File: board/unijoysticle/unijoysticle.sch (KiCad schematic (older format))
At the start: 9 parts, among them J1 DB9_Female_MountingHoles, J2 DB9_Female_MountingHoles, J3 Barrel_Jack_MountingPin, U1 4066, U2 4066, U4 4066, U5 4066

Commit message: board: using switch for c64/amiga mouse
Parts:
- added SW1: SW_SPDT, Button_Switch_THT:SW_CuK_OS102011MA1QN1_SPDT_Angled, symbol Switch:SW_SPDT
- B1: footprint RF_Module:ESP32-WROOM-32 -> Parts:MH-ET_LIVE_MINIKIT_ESP32
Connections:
- net labels added: J1POWER, POWER_OR_GND
- net labels removed: +5V
- wire segments 42 -> 41
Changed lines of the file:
@@
 Wire Wire Line
 	1800 6900 2050 6900
-$Comp
-L power:+5V #PWR08
-U 1 1 5C693B07
-P 2350 6900
-F 0 "#PWR08" H 2350 6750 50  0001 C CNN
-F 1 "+5V" V 2365 7028 50  0000 L CNN
-F 2 "" H 2350 6900 50  0001 C CNN
-F 3 "" H 2350 6900 50  0001 C CNN
-	1    2350 6900
-	0    1    -1   0
-$EndComp
 Text GLabel 2250 1800 2    50   Input ~ 0
 GPIO_J1DOWN
@@
 Wire Wire Line
 	3650 1250 2950 1250
-$Comp
-L power:VDD #PWR0103
-U 1 1 5C6D9076
-P 2950 1250
-F 0 "#PWR0103" H 2950 1100 50  0001 C CNN
-F 1 "VDD" V 2967 1377 50  0000 L CNN
-F 2 "" H 2950 1250 50  0001 C CNN
-F 3 "" H 2950 1250 50  0001 C CNN
-	1    2950 1250
-	0    -1   1    0
-$EndComp
 Text GLabel 6800 950  2    50   Input ~ 0
 J2UP
@@
 Wire Wire Line
 	7300 1450 6800 1450
-Wire Wire Line
-	6800 1250 7300 1250
-$Comp
-L power:VDD #PWR0104
-U 1 1 5C6DCA05
-P 7300 1250
-F 0 "#PWR0104" H 7300 1100 50  0001 C CNN
-F 1 "VDD" V 7317 1378 50  0000 L CNN
-F 2 "" H 7300 1250 50  0001 C CNN
-F 3 "" H 7300 1250 50  0001 C CNN
-	1    7300 1250
-	0    1    1    0
-$EndComp
 Text GLabel 8250 950  0    50   Input ~ 0
 J2UP
@@
 	9250 4250 9450 4250
 Connection ~ 9250 4250
-$Comp
-L power:VDD #PWR0105
-U 1 1 5C6E6105
-P 9450 4250
-F 0 "#PWR0105" H 9450 4100 50  0001 C CNN
-F 1 "VDD" V 9467 4378 50  0000 L CNN
-F 2 "" H 9450 4250 50  0001 C CNN
-F 3 "" H 9450 4250 50  0001 C CNN
-	1    9450 4250
-	0    1    1    0
-$EndComp
 Text GLabel 2250 3850 2    50   Input ~ 0
 J1FIRE
@@
 Connection ~ 1250 4550
 $Comp
-L power:VDD #PWR0106
-U 1 1 5C6E8414
-P 1100 4550
-F 0 "#PWR0106" H 1100 4400 50  0001 C CNN
-F 1 "VDD" V 1118 4677 50  0000 L CNN
-F 2 "" H 1100 4550 50  0001 C CNN
-F 3 "" H 1100 4550 50  0001 C CNN
-	1    1100 4550
-	0    -1   -1   0
-$EndComp
-$Comp
 L power:GND #PWR0107
 U 1 1 5C6BCB4E
@@
 F 0 "B1" H 5250 5560 45  0000 C CNN
 F 1 "ESP32_THING_W_ANT_KEEPOUT" H 5250 5476 45  0000 C CNN
-F 2 "RF_Module:ESP32-WROOM-32" H 5250 5400 20  0001 C CNN
+F 2 "Parts:MH-ET_LIVE_MINIKIT_ESP32" H 5250 5400 20  0001 C CNN
 F 3 "" H 5250 4200 50  0001 C CNN
 F 4 "DEV-13907" H 5250 5381 60  0000 C CNN "Field4"
@@
 Wire Wire Line
 	4300 5000 4750 5000
-$Comp
-L power:+5V #PWR0108
-U 1 1 5C6C0C34
+Entry Bus Bus
+	8750 7700 8850 7800
+$Comp
+L power:VDD #PWR0103
+U 1 1 5C6BA1C1
+P 2350 6900
+F 0 "#PWR0103" H 2350 6750 50  0001 C CNN
+F 1 "VDD" V 2367 7028 50  0000 L CNN
+F 2 "" H 2350 6900 50  0001 C CNN
+F 3 "" H 2350 6900 50  0001 C CNN
+	1    2350 6900
+	0    1    1    0
+$EndComp
+$Comp
+L power:VDD #PWR0104
+U 1 1 5C6BA444
 P 4300 5000
-F 0 "#PWR0108" H 4300 4850 50  0001 C CNN
-F 1 "+5V" V 4315 5128 50  0000 L CNN
+F 0 "#PWR0104" H 4300 4850 50  0001 C CNN
+F 1 "VDD" V 4318 5127 50  0000 L CNN
 F 2 "" H 4300 5000 50  0001 C CNN
 F 3 "" H 4300 5000 50  0001 C CNN
 	1    4300 5000
-	0    -1   1    0
-$EndComp
+	0    -1   -1   0
+$EndComp
+Text GLabel 2950 1250 0    50   Input ~ 0
+J1POWER
+$Comp
+L Switch:SW_SPDT SW1
+U 1 1 5C6BA76A
+P 1650 5800
+F 0 "SW1" H 1650 6085 50  0000 C CNN
+F 1 "SW_SPDT" H 1650 5994 50  0000 C CNN
+F 2 "Button_Switch_THT:SW_CuK_OS102011MA1QN1_SPDT_Angled" H 1650 5800 50  0001 C CNN
+F 3 "" H 1650 5800 50  0001 C CNN
+	1    1650 5800
+	1    0    0    -1
+$EndComp
+Text GLabel 1850 5900 2    50   Input ~ 0
+J1POWER
+$Comp
+L power:GND #PWR0105
+U 1 1 5C6BAB57
+P 1850 5700
+F 0 "#PWR0105" H 1850 5450 50  0001 C CNN
+F 1 "GND" V 1855 5572 50  0000 R CNN
+F 2 "" H 1850 5700 50  0001 C CNN
+F 3 "" H 1850 5700 50  0001 C CNN
+	1    1850 5700
+	0    -1   -1   0
+$EndComp
+Text GLabel 1450 5800 0    50   Input ~ 0
+POWER_OR_GND
+Text GLabel 1100 4550 0    50   Input ~ 0
+POWER_OR_GND
+Text GLabel 9450 4250 2    50   Input ~ 0
+POWER_OR_GND
 $EndSCHEMATC

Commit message: board: better layout
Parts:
- J1: footprint Connector_Dsub:DSUB-9_Female_Horizontal_P2.77x2.84mm_EdgePinOffset4.94mm_Housed_MountingHolesOffset7.48mm -> Connector_Dsub:DSUB-9_Female_Horizontal_P2.77x2.84mm_EdgePinOffset9.40mm
- J2: footprint Connector_Dsub:DSUB-9_Female_Horizontal_P2.77x2.84mm_EdgePinOffset4.94mm_Housed_MountingHolesOffset7.48mm -> Connector_Dsub:DSUB-9_Female_EdgeMount_P2.77mm
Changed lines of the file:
@@
 F 0 "J1" H 4130 1353 50  0000 L CNN
 F 1 "DB9_Female_MountingHoles" H 4130 1262 50  0000 L CNN
-F 2 "Connector_Dsub:DSUB-9_Female_Horizontal_P2.77x2.84mm_EdgePinOffset4.94mm_Housed_MountingHolesOffset7.48mm" H 3950 1350 50  0001 C CNN
+F 2 "Connector_Dsub:DSUB-9_Female_Horizontal_P2.77x2.84mm_EdgePinOffset9.40mm" H 3950 1350 50  0001 C CNN
 F 3 " ~" H 3950 1350 50  0001 C CNN
 	1    3950 1350
@@
 F 0 "J2" H 6680 1353 50  0000 L CNN
 F 1 "DB9_Female_MountingHoles" H 6680 1262 50  0000 L CNN
-F 2 "Connector_Dsub:DSUB-9_Female_Horizontal_P2.77x2.84mm_EdgePinOffset4.94mm_Housed_MountingHolesOffset7.48mm" H 6500 1350 50  0001 C CNN
+F 2 "Connector_Dsub:DSUB-9_Female_EdgeMount_P2.77mm" H 6500 1350 50  0001 C CNN
 F 3 " ~" H 6500 1350 50  0001 C CNN
 	1    6500 1350

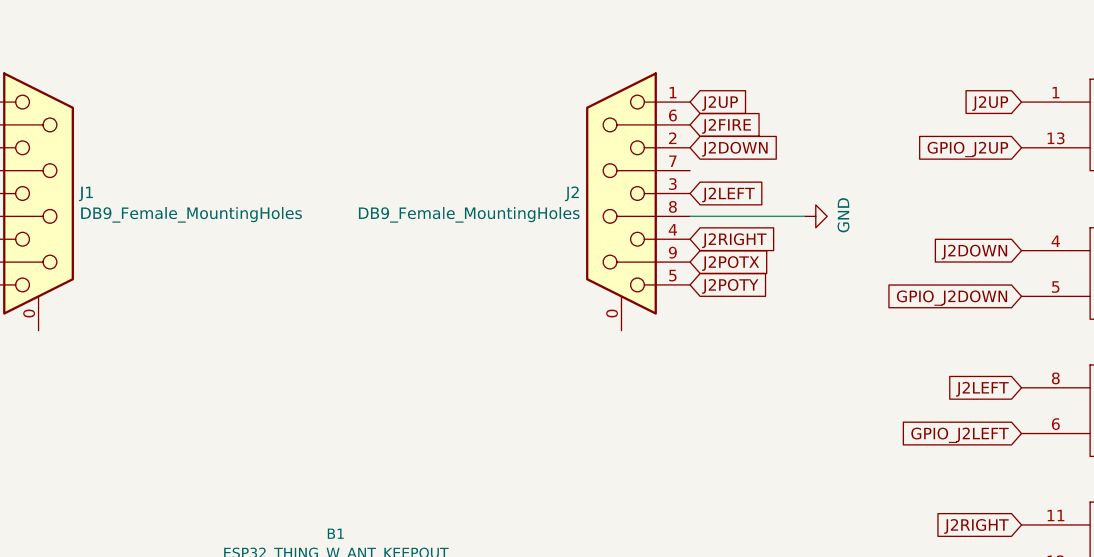
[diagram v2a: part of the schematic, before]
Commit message: board: routing added
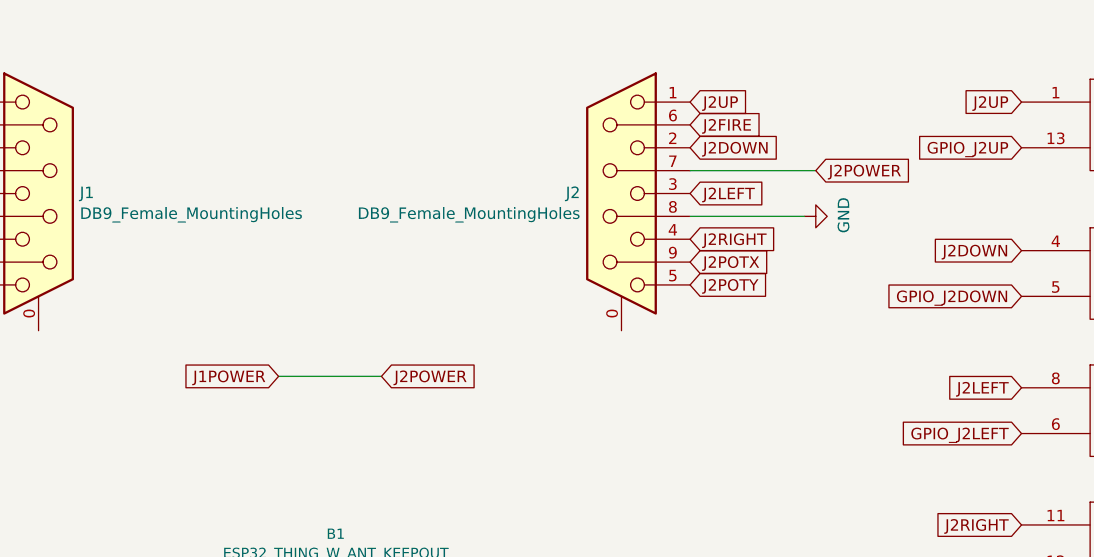
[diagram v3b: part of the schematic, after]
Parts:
- J2: footprint Connector_Dsub:DSUB-9_Female_EdgeMount_P2.77mm -> Connector_Dsub:DSUB-9_Female_Horizontal_P2.77x2.84mm_EdgePinOffset9.40mm
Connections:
- net J1POWER: now also J2.7
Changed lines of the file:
@@
 F 0 "J2" H 6680 1353 50  0000 L CNN
 F 1 "DB9_Female_MountingHoles" H 6680 1262 50  0000 L CNN
-F 2 "Connector_Dsub:DSUB-9_Female_EdgeMount_P2.77mm" H 6500 1350 50  0001 C CNN
+F 2 "Connector_Dsub:DSUB-9_Female_Horizontal_P2.77x2.84mm_EdgePinOffset9.40mm" H 6500 1350 50  0001 C CNN
 F 3 " ~" H 6500 1350 50  0001 C CNN
 	1    6500 1350
@@
 Text GLabel 9450 4250 2    50   Input ~ 0
 POWER_OR_GND
+Text GLabel 7350 1250 2    50   Input ~ 0
+J2POWER
+Wire Wire Line
+	6800 1250 7350 1250
+Text GLabel 5000 2150 0    50   Input ~ 0
+J1POWER
+Wire Wire Line
+	5000 2150 5450 2150
+Text GLabel 5450 2150 2    50   Input ~ 0
+J2POWER
 $EndSCHEMATC

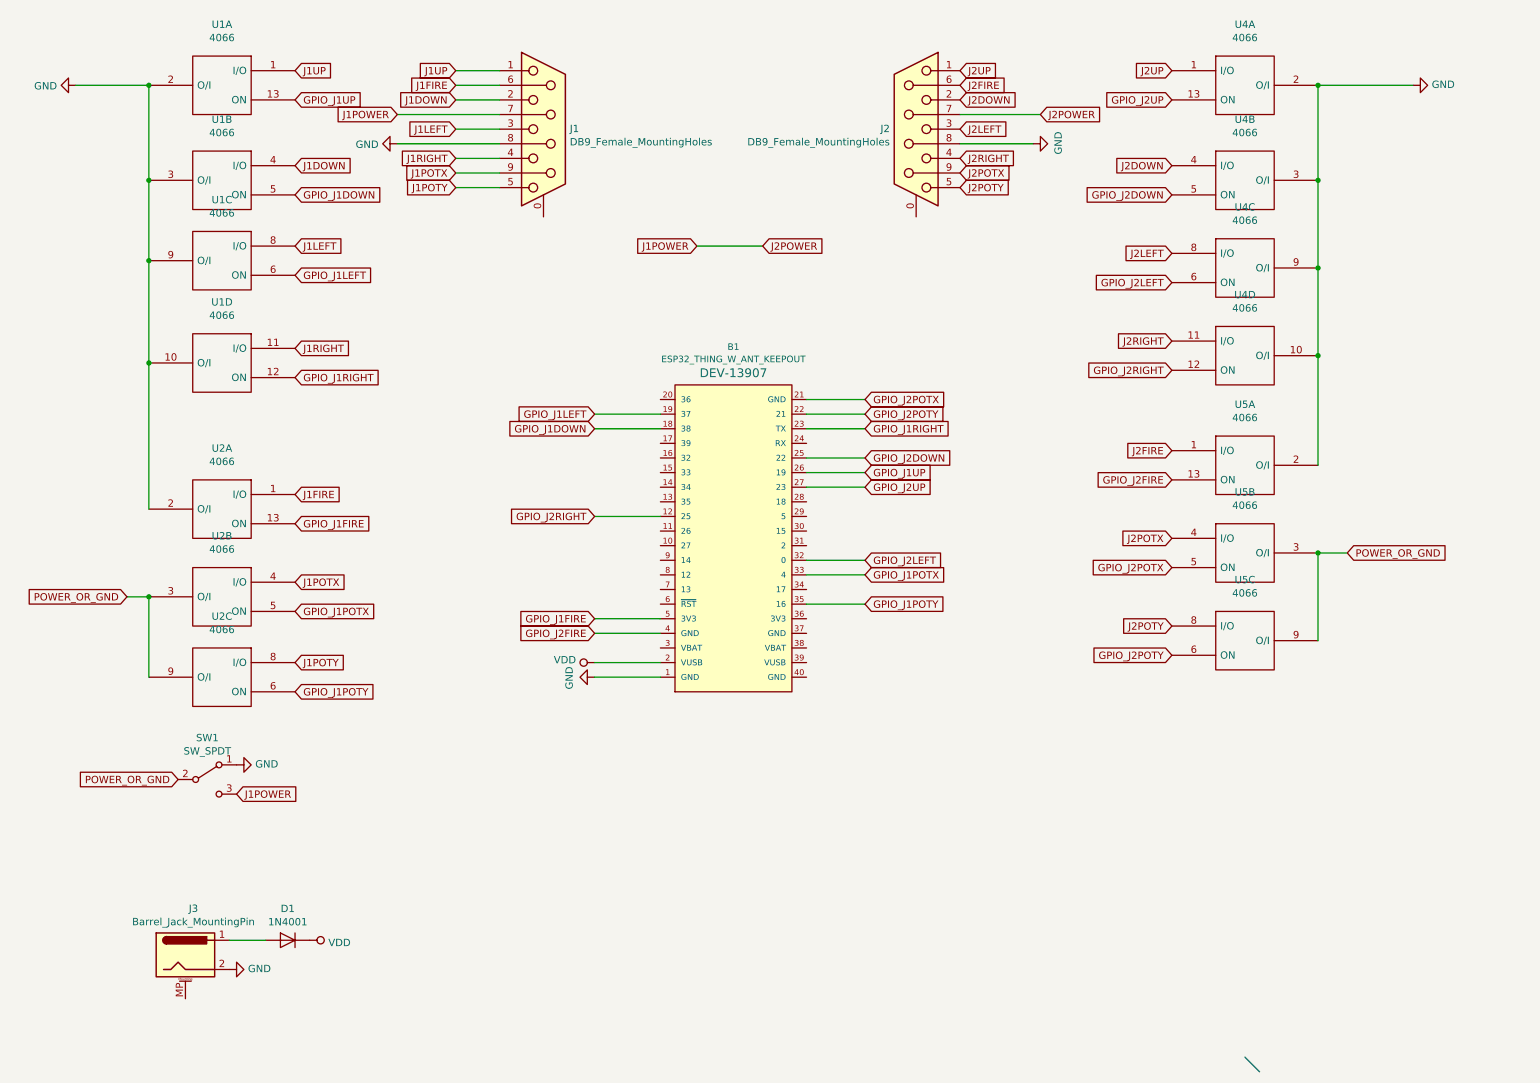
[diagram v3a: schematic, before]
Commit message: board: using new db9 female to avoid errors.
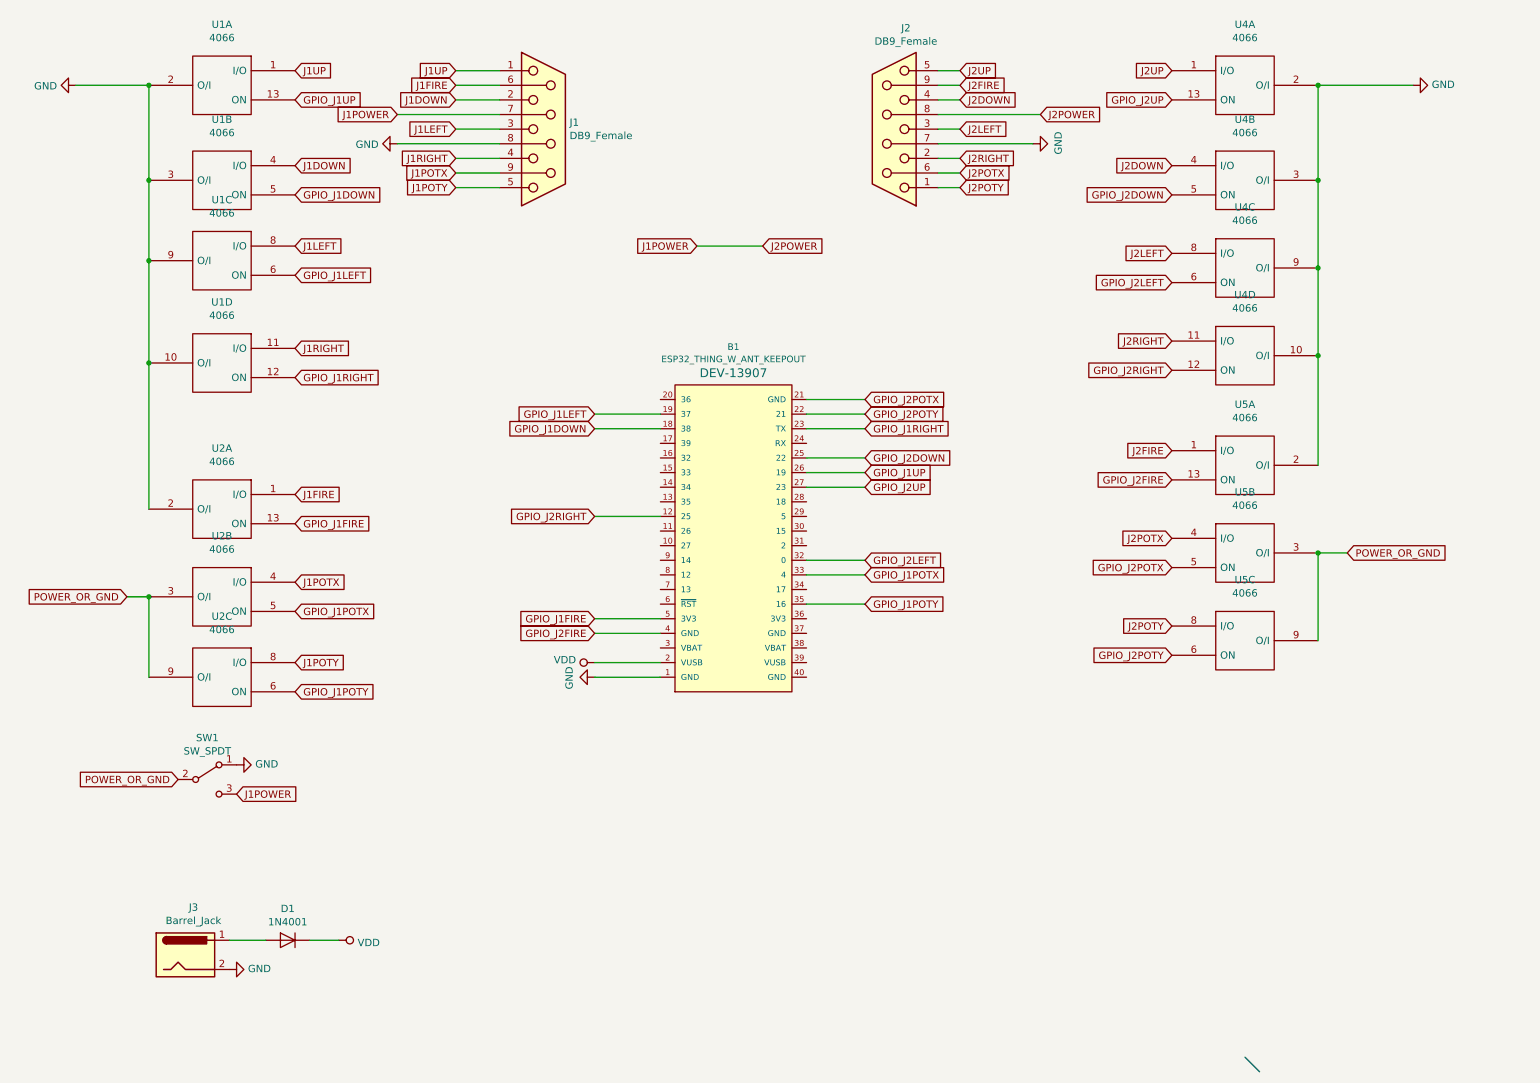
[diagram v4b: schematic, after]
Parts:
- removed J1, J2: DB9_Female_MountingHoles, Connector_Dsub:DSUB-9_Female_Horizontal_P2.77x2.84mm_EdgePinOffset9.40mm, symbol Connector:DB9_Female_MountingHoles
- removed J3: Barrel_Jack_MountingPin, Connector_BarrelJack:BarrelJack_Horizontal, symbol Connector:Barrel_Jack_MountingPin
- added J1, J2: DB9_Female, Connector_Dsub:DSUB-9_Female_Horizontal_P2.77x2.84mm_EdgePinOffset9.40mm, symbol Connector:DB9_Female
- added J3: Barrel_Jack, Connector_BarrelJack:BarrelJack_Horizontal, symbol Connector:Barrel_Jack
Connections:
- net GND: now also J1.8, J2.7, J3.2
- net J1DOWN: now also J1.2
- net J1FIRE: now also J1.6
- net J1LEFT: now also J1.3
- net J1POTX: now also J1.9
- net J1POTY: now also J1.5
- net J1POWER: now also J1.7, J2.8
- net J1RIGHT: now also J1.4
- net J1UP: now also J1.1
- net J2DOWN: now also J2.4
- net J2FIRE: now also J2.9
- net J2LEFT: now also J2.3
- net J2POTX: now also J2.6
- net J2POTY: now also J2.1
- net J2RIGHT: now also J2.2
- net J2UP: now also J2.5
- net at D1.2 (A): now also J3.1
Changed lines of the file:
@@
-$EndComp
-$Comp
-L Connector:DB9_Female_MountingHoles J1
-U 1 1 5C65A0B0
-P 3950 1350
-F 0 "J1" H 4130 1353 50  0000 L CNN
-F 1 "DB9_Female_MountingHoles" H 4130 1262 50  0000 L CNN
-F 2 "Connector_Dsub:DSUB-9_Female_Horizontal_P2.77x2.84mm_EdgePinOffset9.40mm" H 3950 1350 50  0001 C CNN
-F 3 " ~" H 3950 1350 50  0001 C CNN
-	1    3950 1350
-	1    0    0    -1
-$EndComp
-$Comp
-L Connector:DB9_Female_MountingHoles J2
-U 1 1 5C65A122
-P 6500 1350
-F 0 "J2" H 6680 1353 50  0000 L CNN
-F 1 "DB9_Female_MountingHoles" H 6680 1262 50  0000 L CNN
-F 2 "Connector_Dsub:DSUB-9_Female_Horizontal_P2.77x2.84mm_EdgePinOffset9.40mm" H 6500 1350 50  0001 C CNN
-F 3 " ~" H 6500 1350 50  0001 C CNN
-	1    6500 1350
-	-1   0    0    -1
-$EndComp
-$Comp
-L Connector:Barrel_Jack_MountingPin J3
-U 1 1 5C65A2B3
-P 1500 7000
-F 0 "J3" H 1555 7317 50  0000 C CNN
-F 1 "Barrel_Jack_MountingPin" H 1555 7226 50  0000 C CNN
-F 2 "Connector_BarrelJack:BarrelJack_Horizontal" H 1550 6960 50  0001 C CNN
-F 3 "~" H 1550 6960 50  0001 C CNN
-	1    1500 7000
-	1    0    0    -1
 $EndComp
 $Comp
@@
 Text GLabel 6800 1650 2    50   Input ~ 0
 J2POTX
-Wire Wire Line
-	7300 1450 6800 1450
 Text GLabel 8250 950  0    50   Input ~ 0
 J2UP
@@
 L power:VDD #PWR0103
 U 1 1 5C6BA1C1
-P 2350 6900
-F 0 "#PWR0103" H 2350 6750 50  0001 C CNN
-F 1 "VDD" V 2367 7028 50  0000 L CNN
-F 2 "" H 2350 6900 50  0001 C CNN
-F 3 "" H 2350 6900 50  0001 C CNN
-	1    2350 6900
+P 2550 6900
+F 0 "#PWR0103" H 2550 6750 50  0001 C CNN
+F 1 "VDD" V 2567 7028 50  0000 L CNN
+F 2 "" H 2550 6900 50  0001 C CNN
+F 3 "" H 2550 6900 50  0001 C CNN
+	1    2550 6900
 	0    1    1    0
-$EndComp
-$Comp
-L power:VDD #PWR0104
-U 1 1 5C6BA444
-P 4300 5000
-F 0 "#PWR0104" H 4300 4850 50  0001 C CNN
-F 1 "VDD" V 4318 5127 50  0000 L CNN
-F 2 "" H 4300 5000 50  0001 C CNN
-F 3 "" H 4300 5000 50  0001 C CNN
-	1    4300 5000
-	0    -1   -1   0
 $EndComp
 Text GLabel 2950 1250 0    50   Input ~ 0
@@
 Text GLabel 7350 1250 2    50   Input ~ 0
 J2POWER
-Wire Wire Line
-	6800 1250 7350 1250
 Text GLabel 5000 2150 0    50   Input ~ 0
 J1POWER
@@
 Text GLabel 5450 2150 2    50   Input ~ 0
 J2POWER
+$Comp
+L Connector:Barrel_Jack J3
+U 1 1 5C70344B
+P 1500 7000
+F 0 "J3" H 1555 7325 50  0000 C CNN
+F 1 "Barrel_Jack" H 1555 7234 50  0000 C CNN
+F 2 "Connector_BarrelJack:BarrelJack_Horizontal" H 1550 6960 50  0001 C CNN
+F 3 "~" H 1550 6960 50  0001 C CNN
+	1    1500 7000
+	1    0    0    -1
+$EndComp
+$Comp
+L power:VDD #PWR0104
+U 1 1 5C703EAD
+P 4300 5000
+F 0 "#PWR0104" H 4300 4850 50  0001 C CNN
+F 1 "VDD" V 4318 5127 50  0000 L CNN
+F 2 "" H 4300 5000 50  0001 C CNN
+F 3 "" H 4300 5000 50  0001 C CNN
+	1    4300 5000
+	0    -1   -1   0
+$EndComp
+Wire Wire Line
+	2350 6900 2550 6900
+$Comp
+L Connector:DB9_Female J1
+U 1 1 5C705949
+P 3950 1350
+F 0 "J1" H 4129 1396 50  0000 L CNN
+F 1 "DB9_Female" H 4129 1305 50  0000 L CNN
+F 2 "Connector_Dsub:DSUB-9_Female_Horizontal_P2.77x2.84mm_EdgePinOffset9.40mm" H 3950 1350 50  0001 C CNN
+F 3 " ~" H 3950 1350 50  0001 C CNN
+	1    3950 1350
+	1    0    0    -1
+$EndComp
+$Comp
+L Connector:DB9_Female J2
+U 1 1 5C705C0F
+P 6350 1350
+F 0 "J2" H 6270 658 50  0000 C CNN
+F 1 "DB9_Female" H 6270 749 50  0000 C CNN
+F 2 "Connector_Dsub:DSUB-9_Female_Horizontal_P2.77x2.84mm_EdgePinOffset9.40mm" H 6350 1350 50  0001 C CNN
+F 3 " ~" H 6350 1350 50  0001 C CNN
+	1    6350 1350
+	-1   0    0    1
+$EndComp
+Wire Wire Line
+	6650 950  6800 950
+Wire Wire Line
+	6650 1050 6800 1050
+Wire Wire Line
+	6650 1150 6800 1150
+Wire Wire Line
+	6650 1250 7350 1250
+Wire Wire Line
+	6800 1350 6650 1350
+Wire Wire Line
+	6650 1450 7300 1450
+Wire Wire Line
+	6800 1550 6650 1550
+Wire Wire Line
+	6650 1650 6800 1650
+Wire Wire Line
+	6800 1750 6650 1750
 $EndSCHEMATC
